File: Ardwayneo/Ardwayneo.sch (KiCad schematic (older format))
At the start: 10 parts

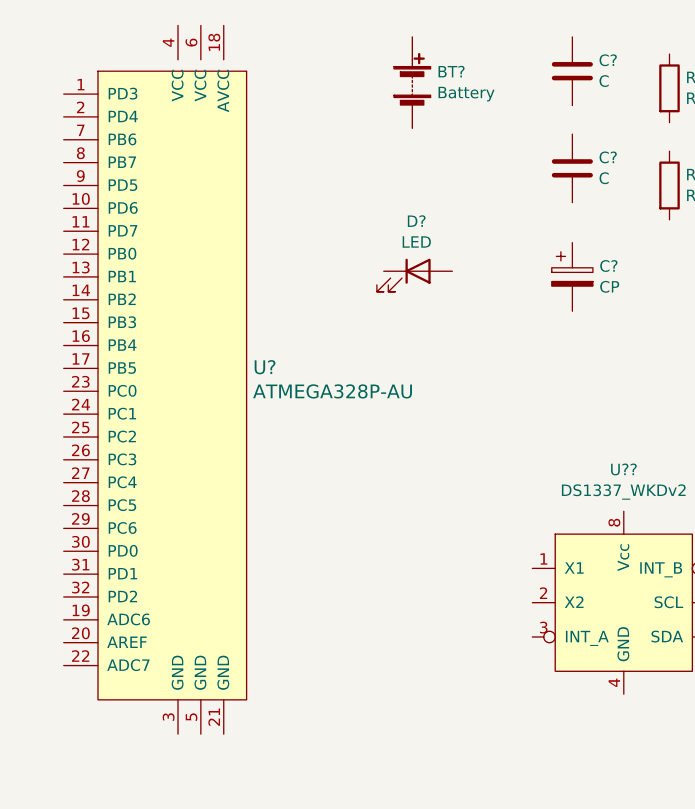
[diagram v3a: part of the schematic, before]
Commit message: Added missing crystal oscillators
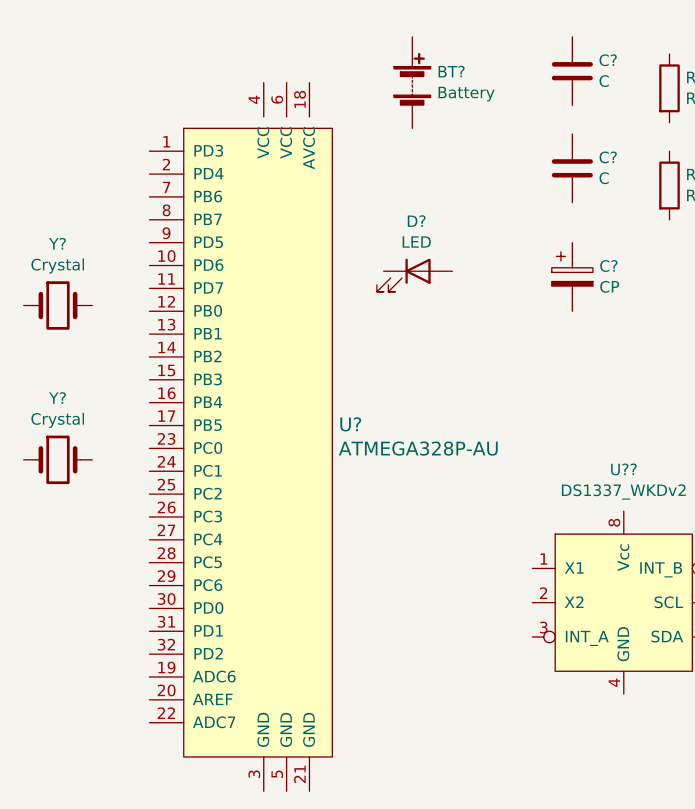
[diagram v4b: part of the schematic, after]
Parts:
- added Y? (x2): Crystal, symbol Device:Crystal
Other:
- moved on the sheet: U?
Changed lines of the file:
@@
 L dk_Embedded-Microcontrollers:ATMEGA328P-AU U?
 U 1 1 5FF24782
-P 1400 4225
-F 0 "U?" H 1728 4328 60  0000 L CNN
-F 1 "ATMEGA328P-AU" H 1728 4222 60  0000 L CNN
-F 2 "digikey-footprints:TQFP-32_7x7mm" H 1600 4425 60  0001 L CNN
-F 3 "http://www.microchip.com/mymicrochip/filehandler.aspx?ddocname=en608326" H 1600 4525 60  0001 L CNN
-F 4 "ATMEGA328P-AU-ND" H 1600 4625 60  0001 L CNN "Digi-Key_PN"
-F 5 "ATMEGA328P-AU" H 1600 4725 60  0001 L CNN "MPN"
-F 6 "Integrated Circuits (ICs)" H 1600 4825 60  0001 L CNN "Category"
-F 7 "Embedded - Microcontrollers" H 1600 4925 60  0001 L CNN "Family"
-F 8 "http://www.microchip.com/mymicrochip/filehandler.aspx?ddocname=en608326" H 1600 5025 60  0001 L CNN "DK_Datasheet_Link"
-F 9 "/product-detail/en/microchip-technology/ATMEGA328P-AU/ATMEGA328P-AU-ND/1832260" H 1600 5125 60  0001 L CNN "DK_Detail_Page"
-F 10 "IC MCU 8BIT 32KB FLASH 32TQFP" H 1600 5225 60  0001 L CNN "Description"
-F 11 "Microchip Technology" H 1600 5325 60  0001 L CNN "Manufacturer"
-F 12 "Active" H 1600 5425 60  0001 L CNN "Status"
-	1    1400 4225
+P 1775 4475
+F 0 "U?" H 2103 4578 60  0000 L CNN
+F 1 "ATMEGA328P-AU" H 2103 4472 60  0000 L CNN
+F 2 "digikey-footprints:TQFP-32_7x7mm" H 1975 4675 60  0001 L CNN
+F 3 "http://www.microchip.com/mymicrochip/filehandler.aspx?ddocname=en608326" H 1975 4775 60  0001 L CNN
+F 4 "ATMEGA328P-AU-ND" H 1975 4875 60  0001 L CNN "Digi-Key_PN"
+F 5 "ATMEGA328P-AU" H 1975 4975 60  0001 L CNN "MPN"
+F 6 "Integrated Circuits (ICs)" H 1975 5075 60  0001 L CNN "Category"
+F 7 "Embedded - Microcontrollers" H 1975 5175 60  0001 L CNN "Family"
+F 8 "http://www.microchip.com/mymicrochip/filehandler.aspx?ddocname=en608326" H 1975 5275 60  0001 L CNN "DK_Datasheet_Link"
+F 9 "/product-detail/en/microchip-technology/ATMEGA328P-AU/ATMEGA328P-AU-ND/1832260" H 1975 5375 60  0001 L CNN "DK_Detail_Page"
+F 10 "IC MCU 8BIT 32KB FLASH 32TQFP" H 1975 5475 60  0001 L CNN "Description"
+F 11 "Microchip Technology" H 1975 5575 60  0001 L CNN "Manufacturer"
+F 12 "Active" H 1975 5675 60  0001 L CNN "Status"
+	1    1775 4475
 	1    0    0    -1
 $EndComp
@@
 	1    0    0    -1
 $EndComp
+$Comp
+L Device:Crystal Y?
+U 1 1 5FF30813
+P 875 3850
+F 0 "Y?" H 875 4118 50  0000 C CNN
+F 1 "Crystal" H 875 4027 50  0000 C CNN
+F 2 "" H 875 3850 50  0001 C CNN
+F 3 "~" H 875 3850 50  0001 C CNN
+	1    875  3850
+	1    0    0    -1
+$EndComp
+$Comp
+L Device:Crystal Y?
+U 1 1 5FF313D6
+P 875 4525
+F 0 "Y?" H 875 4793 50  0000 C CNN
+F 1 "Crystal" H 875 4702 50  0000 C CNN
+F 2 "" H 875 4525 50  0001 C CNN
+F 3 "~" H 875 4525 50  0001 C CNN
+	1    875  4525
+	1    0    0    -1
+$EndComp

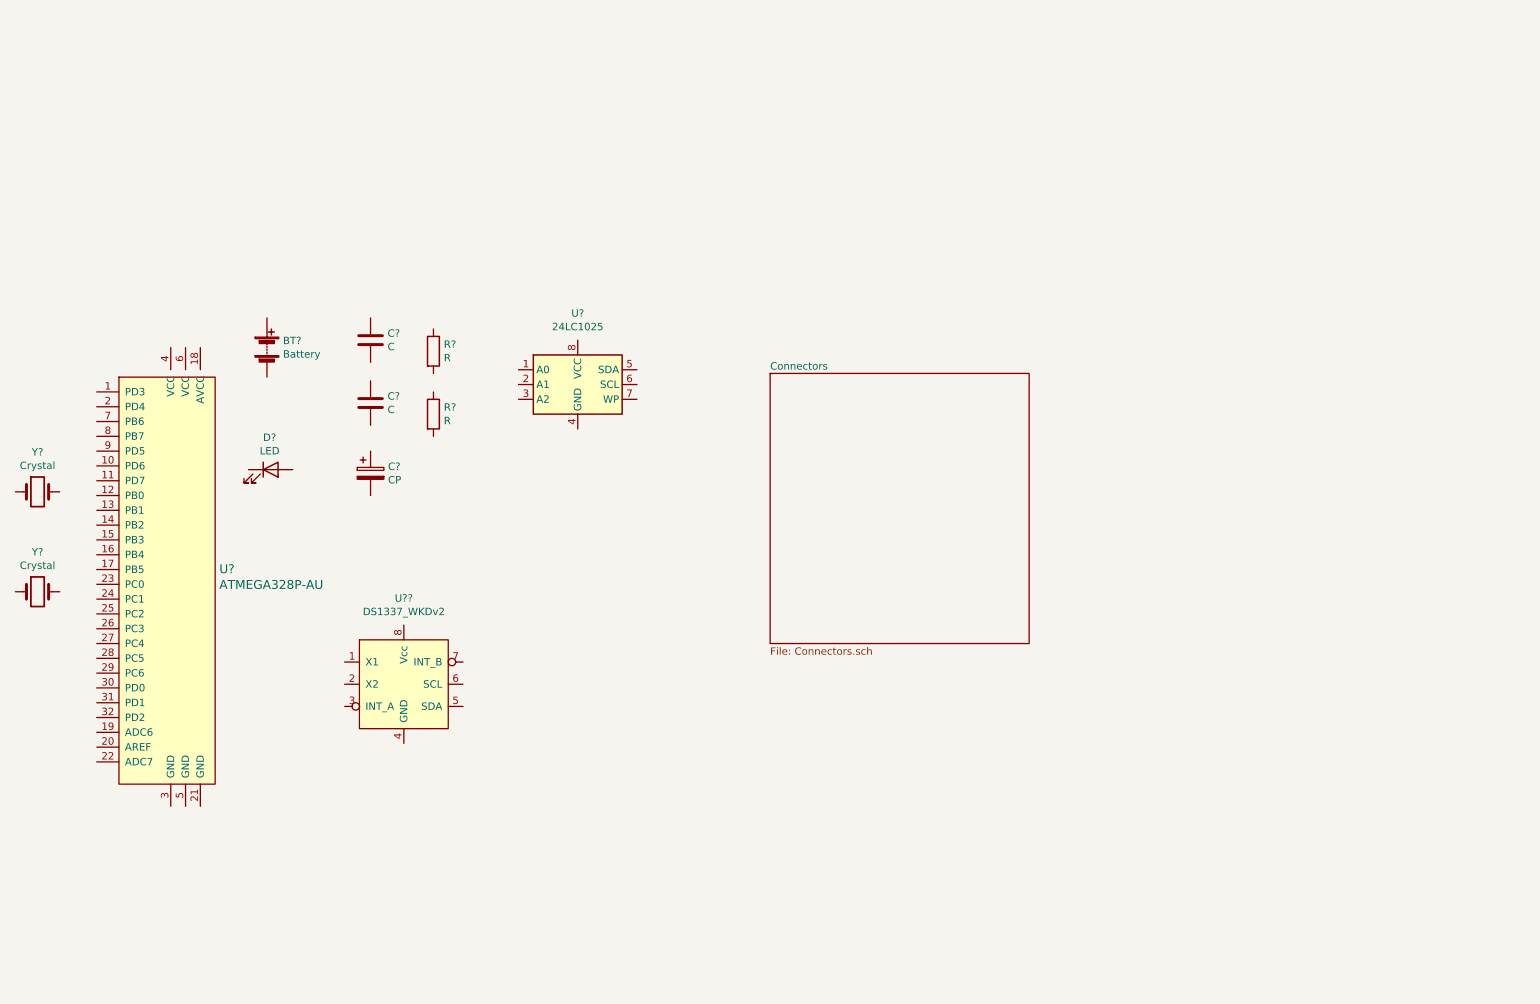
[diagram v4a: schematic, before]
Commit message: Annotation
Annotated all symbols
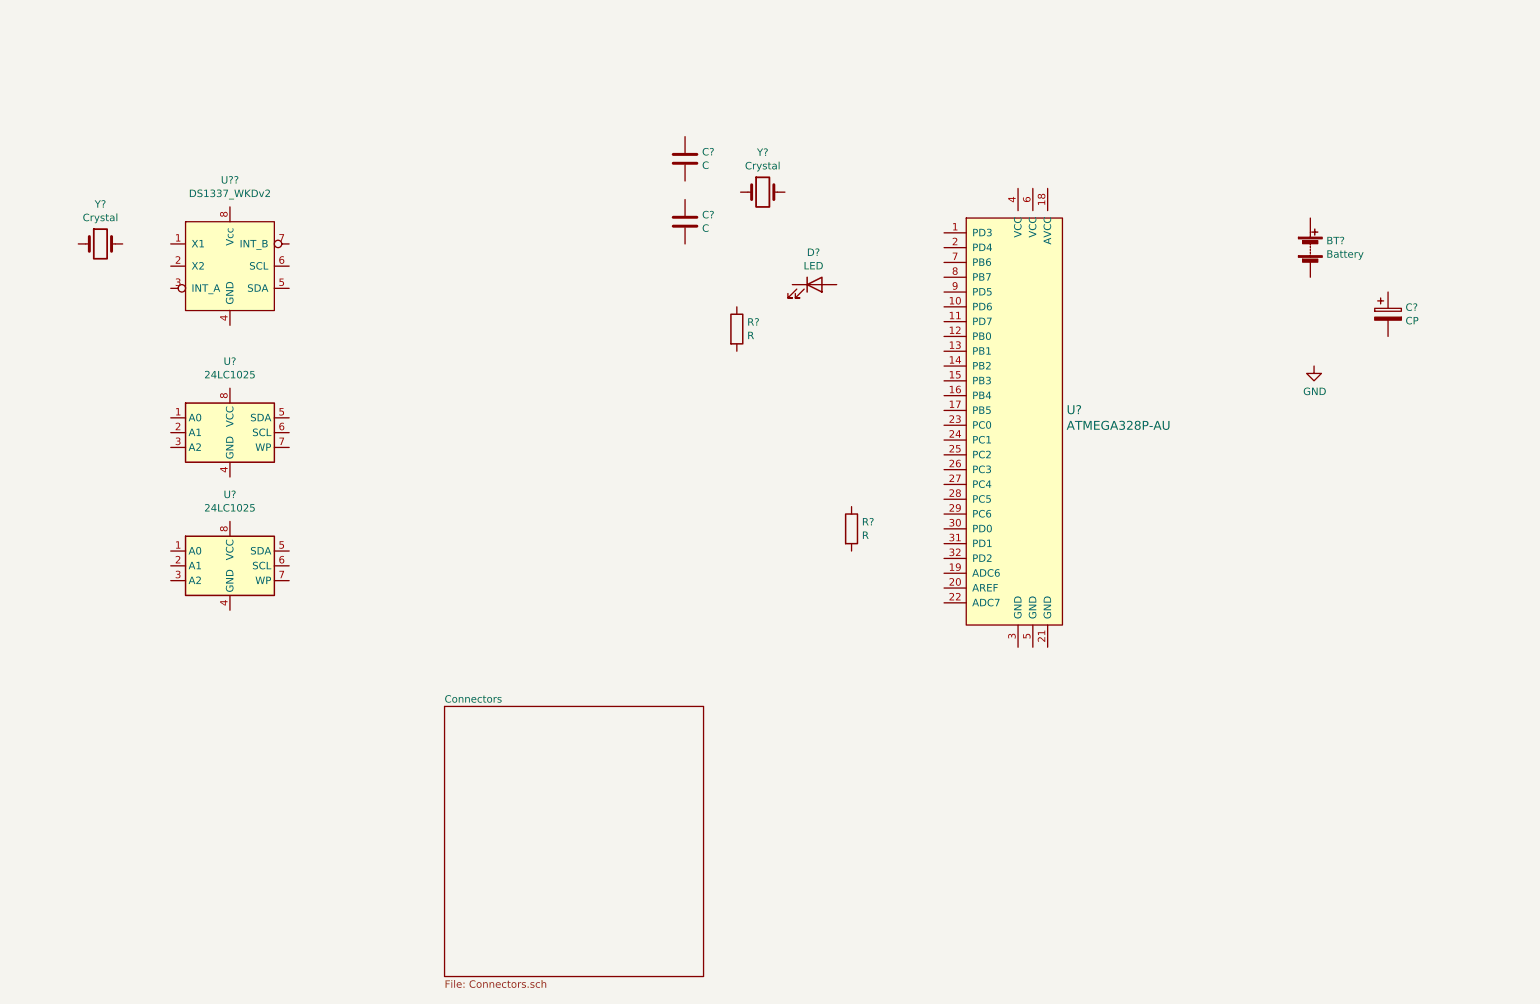
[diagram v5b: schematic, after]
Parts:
- added U?: 24LC1025, symbol Memory_EEPROM:24LC1025
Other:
- moved on the sheet: BT?, C?, D?, R?, U?, U??, Y?
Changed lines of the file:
@@
 L Device:Battery BT?
 U 1 1 5FF1330E
-P 2425 2875
-F 0 "BT?" H 2533 2921 50  0000 L CNN
-F 1 "Battery" H 2533 2830 50  0000 L CNN
-F 2 "" V 2425 2935 50  0001 C CNN
-F 3 "~" V 2425 2935 50  0001 C CNN
-	1    2425 2875
+P 9475 2200
+F 0 "BT?" H 9583 2246 50  0000 L CNN
+F 1 "Battery" H 9583 2155 50  0000 L CNN
+F 2 "" V 9475 2260 50  0001 C CNN
+F 3 "~" V 9475 2260 50  0001 C CNN
+	1    9475 2200
 	1    0    0    -1
 $EndComp
@@
 L Device:C C?
 U 1 1 5FF14682
-P 3125 2825
-F 0 "C?" H 3240 2871 50  0000 L CNN
-F 1 "C" H 3240 2780 50  0000 L CNN
-F 2 "" H 3163 2675 50  0001 C CNN
-F 3 "~" H 3125 2825 50  0001 C CNN
-	1    3125 2825
+P 5250 1600
+F 0 "C?" H 5365 1646 50  0000 L CNN
+F 1 "C" H 5365 1555 50  0000 L CNN
+F 2 "" H 5288 1450 50  0001 C CNN
+F 3 "~" H 5250 1600 50  0001 C CNN
+	1    5250 1600
 	1    0    0    -1
 $EndComp
@@
 L Device:C C?
 U 1 1 5FF15CF4
-P 3125 3250
-F 0 "C?" H 3240 3296 50  0000 L CNN
-F 1 "C" H 3240 3205 50  0000 L CNN
-F 2 "" H 3163 3100 50  0001 C CNN
-F 3 "~" H 3125 3250 50  0001 C CNN
-	1    3125 3250
+P 5250 2025
+F 0 "C?" H 5365 2071 50  0000 L CNN
+F 1 "C" H 5365 1980 50  0000 L CNN
+F 2 "" H 5288 1875 50  0001 C CNN
+F 3 "~" H 5250 2025 50  0001 C CNN
+	1    5250 2025
 	1    0    0    -1
 $EndComp
@@
 L Device:CP C?
 U 1 1 5FF162B4
-P 3125 3725
-F 0 "C?" H 3243 3771 50  0000 L CNN
-F 1 "CP" H 3243 3680 50  0000 L CNN
-F 2 "" H 3163 3575 50  0001 C CNN
-F 3 "~" H 3125 3725 50  0001 C CNN
-	1    3125 3725
+P 10000 2650
+F 0 "C?" H 10118 2696 50  0000 L CNN
+F 1 "CP" H 10118 2605 50  0000 L CNN
+F 2 "" H 10038 2500 50  0001 C CNN
+F 3 "~" H 10000 2650 50  0001 C CNN
+	1    10000 2650
 	1    0    0    -1
 $EndComp
@@
 L Device:LED D?
 U 1 1 5FF17C37
-P 2450 3700
-F 0 "D?" H 2443 3917 50  0000 C CNN
-F 1 "LED" H 2443 3826 50  0000 C CNN
-F 2 "" H 2450 3700 50  0001 C CNN
-F 3 "~" H 2450 3700 50  0001 C CNN
-	1    2450 3700
+P 6125 2450
+F 0 "D?" H 6118 2667 50  0000 C CNN
+F 1 "LED" H 6118 2576 50  0000 C CNN
+F 2 "" H 6125 2450 50  0001 C CNN
+F 3 "~" H 6125 2450 50  0001 C CNN
+	1    6125 2450
 	1    0    0    -1
 $EndComp
@@
 L Device:R R?
 U 1 1 5FF18E03
-P 3550 2900
-F 0 "R?" H 3620 2946 50  0000 L CNN
-F 1 "R" H 3620 2855 50  0000 L CNN
-F 2 "" V 3480 2900 50  0001 C CNN
-F 3 "~" H 3550 2900 50  0001 C CNN
-	1    3550 2900
+P 5600 2750
+F 0 "R?" H 5670 2796 50  0000 L CNN
+F 1 "R" H 5670 2705 50  0000 L CNN
+F 2 "" V 5530 2750 50  0001 C CNN
+F 3 "~" H 5600 2750 50  0001 C CNN
+	1    5600 2750
 	1    0    0    -1
 $EndComp
@@
 L Device:R R?
 U 1 1 5FF1933E
-P 3550 3325
-F 0 "R?" H 3620 3371 50  0000 L CNN
-F 1 "R" H 3620 3280 50  0000 L CNN
-F 2 "" V 3480 3325 50  0001 C CNN
-F 3 "~" H 3550 3325 50  0001 C CNN
-	1    3550 3325
+P 6375 4100
+F 0 "R?" H 6445 4146 50  0000 L CNN
+F 1 "R" H 6445 4055 50  0000 L CNN
+F 2 "" V 6305 4100 50  0001 C CNN
+F 3 "~" H 6375 4100 50  0001 C CNN
+	1    6375 4100
 	1    0    0    -1
 $EndComp
@@
 L Memory_EEPROM:24LC1025 U?
 U 1 1 5FF1A37B
-P 4525 3125
-F 0 "U?" H 4525 3606 50  0000 C CNN
-F 1 "24LC1025" H 4525 3515 50  0000 C CNN
-F 2 "" H 4525 3125 50  0001 C CNN
-F 3 "http://ww1.microchip.com/downloads/en/DeviceDoc/21941B.pdf" H 4525 3125 50  0001 C CNN
-	1    4525 3125
+P 2175 3450
+F 0 "U?" H 2175 3931 50  0000 C CNN
+F 1 "24LC1025" H 2175 3840 50  0000 C CNN
+F 2 "" H 2175 3450 50  0001 C CNN
+F 3 "http://ww1.microchip.com/downloads/en/DeviceDoc/21941B.pdf" H 2175 3450 50  0001 C CNN
+	1    2175 3450
 	1    0    0    -1
 $EndComp
 $Sheet
-S 5825 3050 1750 1825
+S 3625 5300 1750 1825
 U 5FF1D20B
 F0 "Connectors" 50
@@
 L dk_Embedded-Microcontrollers:ATMEGA328P-AU U?
 U 1 1 5FF24782
-P 1775 4475
-F 0 "U?" H 2103 4578 60  0000 L CNN
-F 1 "ATMEGA328P-AU" H 2103 4472 60  0000 L CNN
-F 2 "digikey-footprints:TQFP-32_7x7mm" H 1975 4675 60  0001 L CNN
-F 3 "http://www.microchip.com/mymicrochip/filehandler.aspx?ddocname=en608326" H 1975 4775 60  0001 L CNN
-F 4 "ATMEGA328P-AU-ND" H 1975 4875 60  0001 L CNN "Digi-Key_PN"
-F 5 "ATMEGA328P-AU" H 1975 4975 60  0001 L CNN "MPN"
-F 6 "Integrated Circuits (ICs)" H 1975 5075 60  0001 L CNN "Category"
-F 7 "Embedded - Microcontrollers" H 1975 5175 60  0001 L CNN "Family"
-F 8 "http://www.microchip.com/mymicrochip/filehandler.aspx?ddocname=en608326" H 1975 5275 60  0001 L CNN "DK_Datasheet_Link"
-F 9 "/product-detail/en/microchip-technology/ATMEGA328P-AU/ATMEGA328P-AU-ND/1832260" H 1975 5375 60  0001 L CNN "DK_Detail_Page"
-F 10 "IC MCU 8BIT 32KB FLASH 32TQFP" H 1975 5475 60  0001 L CNN "Description"
-F 11 "Microchip Technology" H 1975 5575 60  0001 L CNN "Manufacturer"
-F 12 "Active" H 1975 5675 60  0001 L CNN "Status"
-	1    1775 4475
+P 7500 3400
+F 0 "U?" H 7828 3503 60  0000 L CNN
+F 1 "ATMEGA328P-AU" H 7828 3397 60  0000 L CNN
+F 2 "digikey-footprints:TQFP-32_7x7mm" H 7700 3600 60  0001 L CNN
+F 3 "http://www.microchip.com/mymicrochip/filehandler.aspx?ddocname=en608326" H 7700 3700 60  0001 L CNN
+F 4 "ATMEGA328P-AU-ND" H 7700 3800 60  0001 L CNN "Digi-Key_PN"
+F 5 "ATMEGA328P-AU" H 7700 3900 60  0001 L CNN "MPN"
+F 6 "Integrated Circuits (ICs)" H 7700 4000 60  0001 L CNN "Category"
+F 7 "Embedded - Microcontrollers" H 7700 4100 60  0001 L CNN "Family"
+F 8 "http://www.microchip.com/mymicrochip/filehandler.aspx?ddocname=en608326" H 7700 4200 60  0001 L CNN "DK_Datasheet_Link"
+F 9 "/product-detail/en/microchip-technology/ATMEGA328P-AU/ATMEGA328P-AU-ND/1832260" H 7700 4300 60  0001 L CNN "DK_Detail_Page"
+F 10 "IC MCU 8BIT 32KB FLASH 32TQFP" H 7700 4400 60  0001 L CNN "Description"
+F 11 "Microchip Technology" H 7700 4500 60  0001 L CNN "Manufacturer"
+F 12 "Active" H 7700 4600 60  0001 L CNN "Status"
+	1    7500 3400
 	1    0    0    -1
 $EndComp
@@
 L Ardwayneo_Library:DS1337_WKDv2 U??
 U 1 1 5FF2FA48
-P 3350 5150
-F 0 "U??" H 3350 5731 50  0000 C CNN
-F 1 "DS1337_WKDv2" H 3350 5640 50  0000 C CNN
-F 2 "" H 3350 5150 50  0001 C CNN
-F 3 "https://datasheets.maximintegrated.com/en/ds/DS1337-DS1337C.pdf" H 3350 5150 50  0001 C CNN
-	1    3350 5150
+P 2175 2325
+F 0 "U??" H 2175 2906 50  0000 C CNN
+F 1 "DS1337_WKDv2" H 2175 2815 50  0000 C CNN
+F 2 "" H 2175 2325 50  0001 C CNN
+F 3 "https://datasheets.maximintegrated.com/en/ds/DS1337-DS1337C.pdf" H 2175 2325 50  0001 C CNN
+	1    2175 2325
 	1    0    0    -1
 $EndComp
@@
 L Device:Crystal Y?
 U 1 1 5FF30813
-P 875 3850
-F 0 "Y?" H 875 4118 50  0000 C CNN
-F 1 "Crystal" H 875 4027 50  0000 C CNN
-F 2 "" H 875 3850 50  0001 C CNN
-F 3 "~" H 875 3850 50  0001 C CNN
-	1    875  3850
+P 1300 2175
+F 0 "Y?" H 1300 2443 50  0000 C CNN
+F 1 "Crystal" H 1300 2352 50  0000 C CNN
+F 2 "" H 1300 2175 50  0001 C CNN
+F 3 "~" H 1300 2175 50  0001 C CNN
+	1    1300 2175
 	1    0    0    -1
 $EndComp
@@
 L Device:Crystal Y?
 U 1 1 5FF313D6
-P 875 4525
-F 0 "Y?" H 875 4793 50  0000 C CNN
-F 1 "Crystal" H 875 4702 50  0000 C CNN
-F 2 "" H 875 4525 50  0001 C CNN
-F 3 "~" H 875 4525 50  0001 C CNN
-	1    875  4525
+P 5775 1825
+F 0 "Y?" H 5775 2093 50  0000 C CNN
+F 1 "Crystal" H 5775 2002 50  0000 C CNN
+F 2 "" H 5775 1825 50  0001 C CNN
+F 3 "~" H 5775 1825 50  0001 C CNN
+	1    5775 1825
 	1    0    0    -1
 $EndComp
+$Comp
+L Memory_EEPROM:24LC1025 U?
+U 1 1 5FF3E64A
+P 2175 4350
+F 0 "U?" H 2175 4831 50  0000 C CNN
+F 1 "24LC1025" H 2175 4740 50  0000 C CNN
+F 2 "" H 2175 4350 50  0001 C CNN
+F 3 "http://ww1.microchip.com/downloads/en/DeviceDoc/21941B.pdf" H 2175 4350 50  0001 C CNN
+	1    2175 4350
+	1    0    0    -1
+$EndComp
+$Comp
+L power:GND #PWR?
+U 1 1 5FF53AB3
+P 9500 3000
+F 0 "#PWR?" H 9500 2750 50  0001 C CNN
+F 1 "GND" H 9505 2827 50  0000 C CNN
+F 2 "" H 9500 3000 50  0001 C CNN
+F 3 "" H 9500 3000 50  0001 C CNN
+	1    9500 3000
+	1    0    0    -1
+$EndComp
